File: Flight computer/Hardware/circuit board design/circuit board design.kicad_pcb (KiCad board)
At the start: 4 copper layers, 30.5 x 82.6 mm, 91 parts, among them J1 Conn_01x05, J2 USB_B_Micro, J3 Screw_Terminal_01x04, J4 Conn_01x02, J5 Screw_Terminal_01x04, J6 Conn_Coaxial, J7 Conn_Coaxial, SW1 SW_DPST, U1 IIS2MDC, U10 BMI088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

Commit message: Done extensive routing of the board.
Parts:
- removed SW1: SW_DPST, flight-computer:TerminalBlock_TE_282834-4_1x04_P2.54mm_Horizontal
- J3, J5: value Screw_Terminal_01x04 -> Screw_Terminal_01x06; footprint flight-computer:TerminalBlock_TE_282834-4_1x04_P2.54mm_Horizontal -> flight-computer:TerminalBlock_TE_282834-6_1x06_P2.54mm_Horizontal
- J4: moved to B.Cu
- moved R12 105.5 mm to (276.3, 306.1)
- moved R4 101.0 mm to (261.1, 292.1), turned to 180 degrees
- moved C86 98.8 mm to (266.1, 282.9), turned to 270 degrees
- moved C88 97.9 mm to (263.3, 285.5), turned to 270 degrees
- moved C89 97.9 mm to (276.3, 307.8), turned to 180 degrees
- moved R1 95.8 mm to (276.5, 297.1)
- moved C35 93.7 mm to (261.1, 290.4), turned to 180 degrees
- moved C7 91.1 mm to (276.4, 302.0), turned to 180 degrees
- moved Y3 90.8 mm to (263.8, 282.8), turned to 180 degrees
- moved C36 90.1 mm to (260.0, 283.6), turned to 90 degrees
- moved J1 87.7 mm to (279.8, 296.9)
- moved U15 87.7 mm to (260.9, 287.3), turned to 90 degrees
- moved R28 87.1 mm to (256.1, 277.6)
- moved R29 85.1 mm to (259.2, 277.6)
- moved J4 84.6 mm to (256.5, 287.3), turned to 90 degrees
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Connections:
- ANT1 pad 2: Net-(ANT1-Pad2) -> (no net)
- J2 pad 4: Net-(J2-Pad4) -> (no net)
- J3 pad 2: /pyro_driver/FET_B -> Vdrive
- J3 pad 4: /pyro_driver/FET_A -> /pyro_driver/FET_B
- U1 pad 11: Net-(U1-Pad11) -> (no net)
- U1 pad 12: Net-(U1-Pad12) -> (no net)
- U1 pad 2: Net-(U1-Pad2) -> (no net)
- U10 pad 1: Net-(U10-Pad1) -> (no net)
- U10 pad 13: Net-(U10-Pad13) -> (no net)
- U10 pad 5: Net-(U10-Pad5) -> (no net)
- U11 pad 10: Net-(U11-Pad10) -> (no net)
- U11 pad 12: Net-(U11-Pad12) -> (no net)
- U11 pad 17: /pyro_driver/FIRE_A -> /pyro_driver/FIRE_C
- U11 pad 18: /pyro_driver/FIRE_B -> /pyro_driver/FIRE_D
- U11 pad 19: /pyro_driver/FIRE_C -> /pyro_driver/FIRE_A
- U11 pad 20: /pyro_driver/FIRE_D -> /pyro_driver/FIRE_B
- U11 pad 38: Net-(U11-Pad38) -> (no net)
- U11 pad 39: Net-(U11-Pad39) -> (no net)
- U11 pad 5: Net-(U11-Pad5) -> (no net)
- U11 pad 51: Net-(U11-Pad51) -> (no net)
- U11 pad 55: Net-(U11-Pad55) -> (no net)
- U11 pad 59: Net-(U11-Pad59) -> (no net)
- U11 pad 6: Net-(U11-Pad6) -> (no net)
- U11 pad 60: Net-(U11-Pad60) -> (no net)
- U11 pad 9: Net-(U11-Pad9) -> (no net)
- U14 pad 4: Net-(U14-Pad4) -> (no net)
- U3 pad 10: /MCU/MCU_PA13 -> /MCU/MCU_PA12
- U3 pad 16: Net-(U3-Pad16) -> (no net)
- U3 pad 19: Net-(U3-Pad19) -> (no net)
- U3 pad 20: Net-(U3-Pad20) -> (no net)
- U3 pad 5: Net-(U3-Pad5) -> (no net)
- U3 pad 7: Net-(U3-Pad7) -> (no net)
- U3 pad 9: /MCU/MCU_PA12 -> /MCU/MCU_PA13
- U4 pad 13: Net-(U4-Pad13) -> (no net)
- U4 pad 15: Net-(U4-Pad15) -> (no net)
- U4 pad 5: Net-(U4-Pad5) -> (no net)
- U4 pad 6: Net-(U4-Pad6) -> (no net)
- U8 pad 6: Net-(U8-Pad6) -> (no net)
- X1 pad 1: Net-(X1-Pad1) -> (no net)
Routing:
- net Net-(J3-Pad1): track 0.00 -> 162.0 mm
- net /gps/GPS_SCL: track 0.20 -> 59.6 mm, vias 0 -> 2
- net /gps/GPS_NSAFEBOOT: track 0.00 -> 46.9 mm
- net /sensors/ACCL_RDY: track 0.00 -> 44.5 mm, vias 0 -> 2
- net GND: track 106.6 -> 150.8 mm, vias 35 -> 58
- net /gps/GPS_NRES: track 0.00 -> 39.6 mm, vias 0 -> 2
- net /sensors/GYRO_RDY: track 0.00 -> 38.6 mm, vias 0 -> 2
- net /pyro_driver/FIRE_A: track 0.00 -> 38.2 mm, vias 0 -> 2
- net /MCU/MCU_SCLK4: track 0.00 -> 37.1 mm, vias 0 -> 2
- net /MCU/MCU_PA04: track 0.00 -> 34.3 mm, vias 0 -> 2
- net /MCU/MCU_PB11: track 0.00 -> 33.1 mm, vias 0 -> 2
- net /pyro_driver/FIRE_B: track 0.00 -> 32.9 mm, vias 0 -> 2
- net /MCU/GPS_RXD0: track 0.00 -> 29.4 mm
- net /MCU/ARMED: track 0.00 -> 28.8 mm, vias 0 -> 1
- net Net-(C89-Pad1): track 0.00 -> 27.6 mm, vias 0 -> 2
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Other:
- outline, holes or cut-outs redrawn

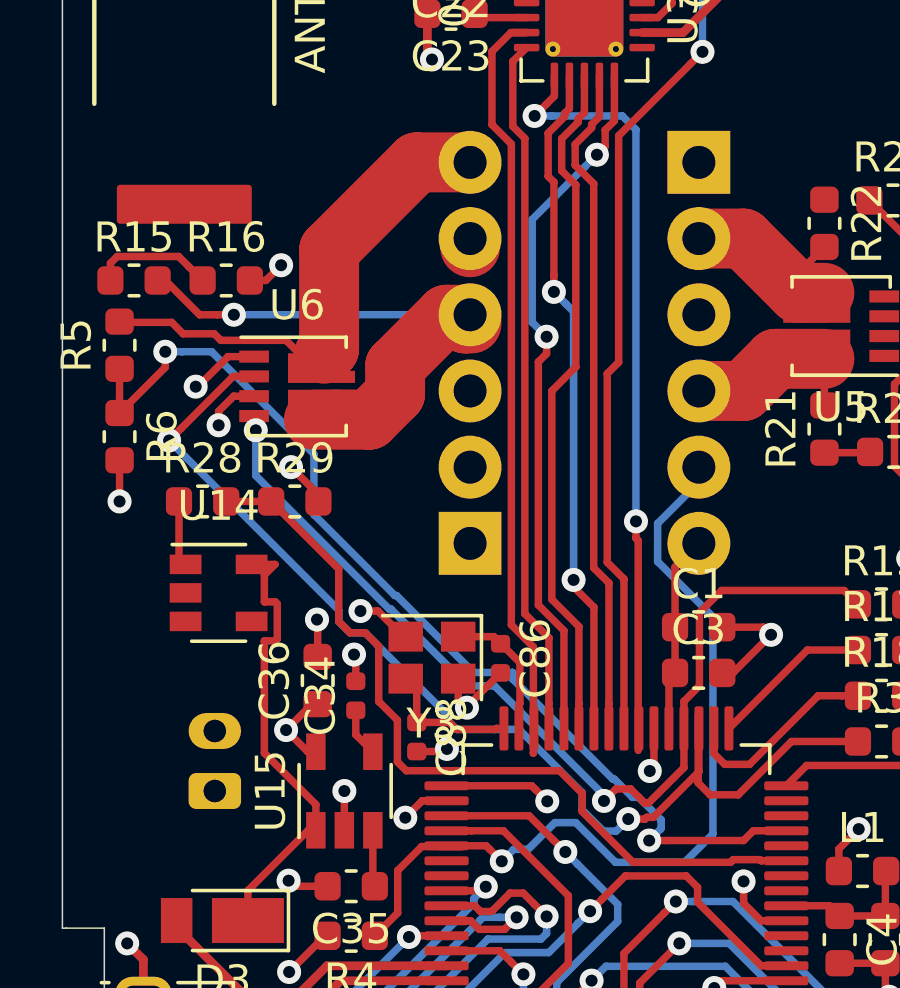
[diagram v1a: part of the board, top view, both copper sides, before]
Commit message: Set up for arming switch
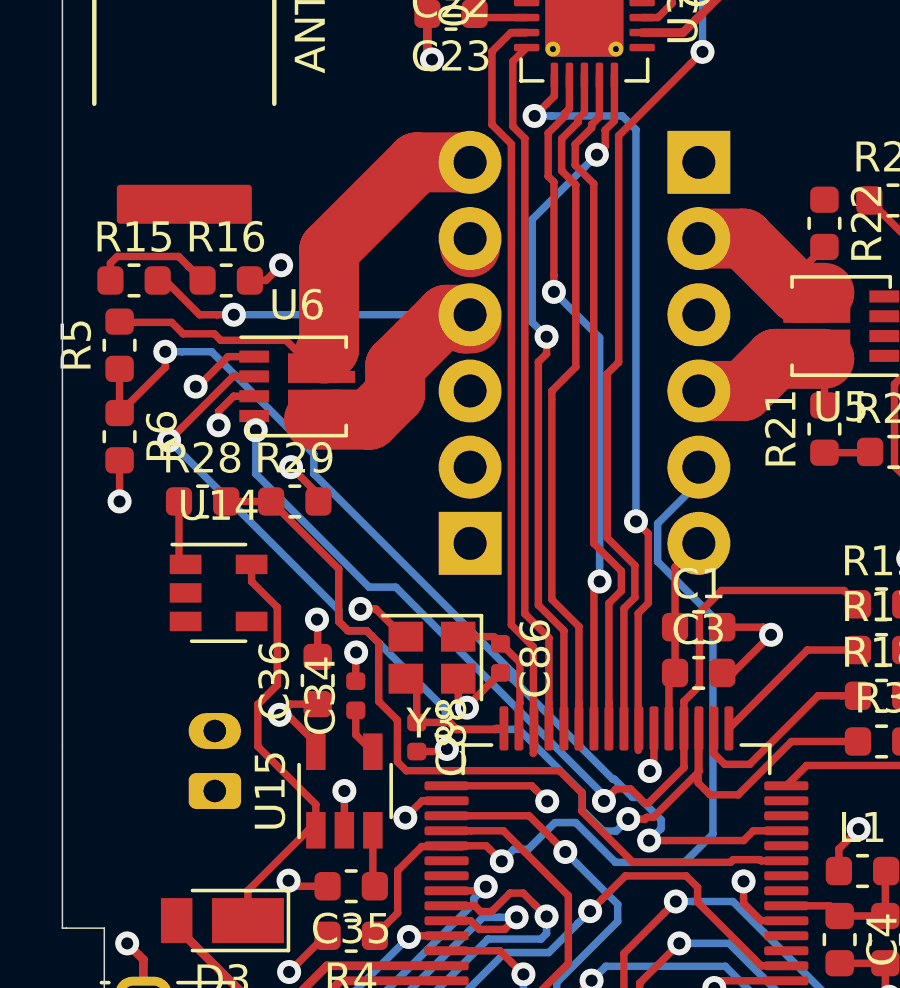
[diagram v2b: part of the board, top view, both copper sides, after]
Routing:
- net Net-(J3-Pad1): track 162.0 -> 0.29 mm
- net Vdrive: track 2.19 -> 24.7 mm
- net Net-(C35-Pad1): track 17.3 -> 16.3 mm
- net /MCU/MCU_PA04: track 34.3 -> 33.5 mm
- net +3V3: track 81.9 -> 82.5 mm

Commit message: only 2 or 3 connections left to route
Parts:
- removed R4: 1K, Resistor_SMD:R_0603_1608Metric
- J3, J5: value Screw_Terminal_01x06 -> Screw_Terminal_01x04; footprint flight-computer:TerminalBlock_TE_282834-6_1x06_P2.54mm_Horizontal -> flight-computer:TerminalBlock_TE_282834-4_1x04_P2.54mm_Horizontal
- moved R2 4.10 mm to (265.8, 322.7), turned to 90 degrees
- moved J5 2.79 mm to (272.7, 269.1)
- moved R21 2.47 mm to (276.4, 277.6), turned to 270 degrees
- moved J3 2.29 mm to (264.9, 276.7)
- moved R23 2.10 mm to (277.9, 277.6), turned to 270 degrees
- moved C8 1.53 mm to (264.8, 322.7)
- moved L8 1.42 mm to (264.3, 257.6)
- moved C22 1.42 mm to (263.0, 259.3)
- moved C9 1.42 mm to (268.6, 252.3)
- moved U3 1.42 mm to (267.5, 261.2)
- moved X1 1.42 mm to (273.9, 256.7)
- moved C19 1.42 mm to (263.4, 255.8)
- moved U2 1.42 mm to (267.6, 255.9)
- moved C20 1.42 mm to (272.4, 259.6)
- moved C21 1.42 mm to (276.2, 256.9)
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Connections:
- J3 pad 1: Net-(J3-Pad1) -> Vdrive
- J3 pad 2: Vdrive -> /pyro_driver/FET_B
- J3 pad 3: Net-(J3-Pad1) -> Vdrive
- J3 pad 4: /pyro_driver/FET_B -> /pyro_driver/FET_A
- J5 pad 1: Net-(J3-Pad1) -> Vdrive
- J5 pad 3: Net-(J3-Pad1) -> Vdrive
- U11 pad 37: /MCU/ARMED -> (no net)
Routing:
- net +3V3: track 82.5 -> 257.7 mm, vias 21 -> 25
- net /MCU/MCU_PA05: track 4.07 -> 33.9 mm, vias 0 -> 2
- net /MCU/ARMED: track 28.8 -> 0.00 mm, vias 1 -> 0
- net Vdrive: track 24.7 -> 5.46 mm, vias 0 -> 2
- net /pyro_driver/FIRE_D: track 6.73 -> 24.2 mm, vias 0 -> 2
- net /MCU/MCU_PA06: track 1.53 -> 18.5 mm, vias 0 -> 2
- net /pyro_driver/FIRE_C: track 5.38 -> 19.7 mm, vias 0 -> 2
- net /pyro_driver/FET_B: track 18.7 -> 4.94 mm, vias 1 -> 0
- net GND: track 150.9 -> 163.8 mm, vias 58 -> 66
- net Net-(C9-Pad1): track 0.00 -> 7.17 mm
- net /MCU/MCU_SCLK4: track 37.1 -> 30.9 mm
- net Net-(C8-Pad1): track 6.56 -> 2.10 mm
- net /pyro_driver/FET_C: track 6.66 -> 10.4 mm
- net Net-(R2-Pad2): track 6.93 -> 3.25 mm
- net /pyro_driver/FET_A: track 16.6 -> 13.7 mm
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- added copper zone on VCC.Cu, net Vdrive
- removed copper zone on VCC.Cu, net +3V3

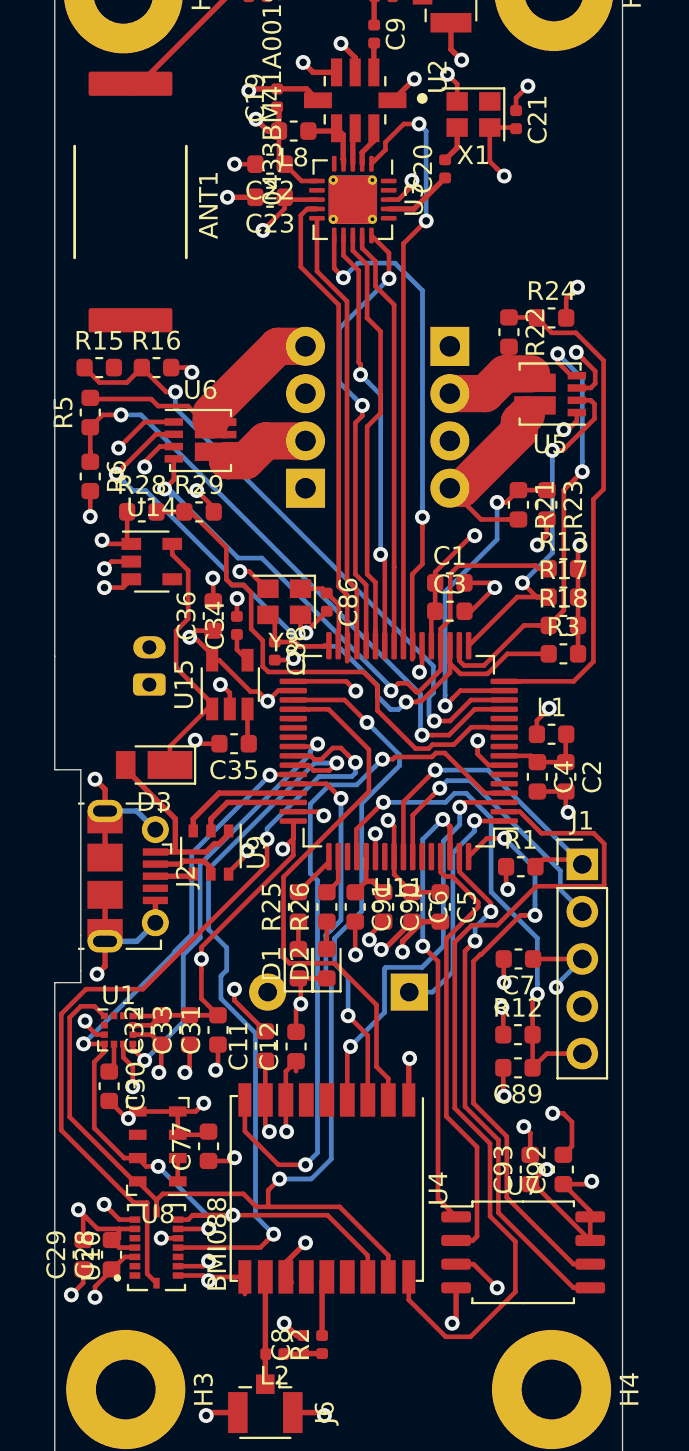
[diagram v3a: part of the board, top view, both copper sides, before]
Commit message: All connections routed!!
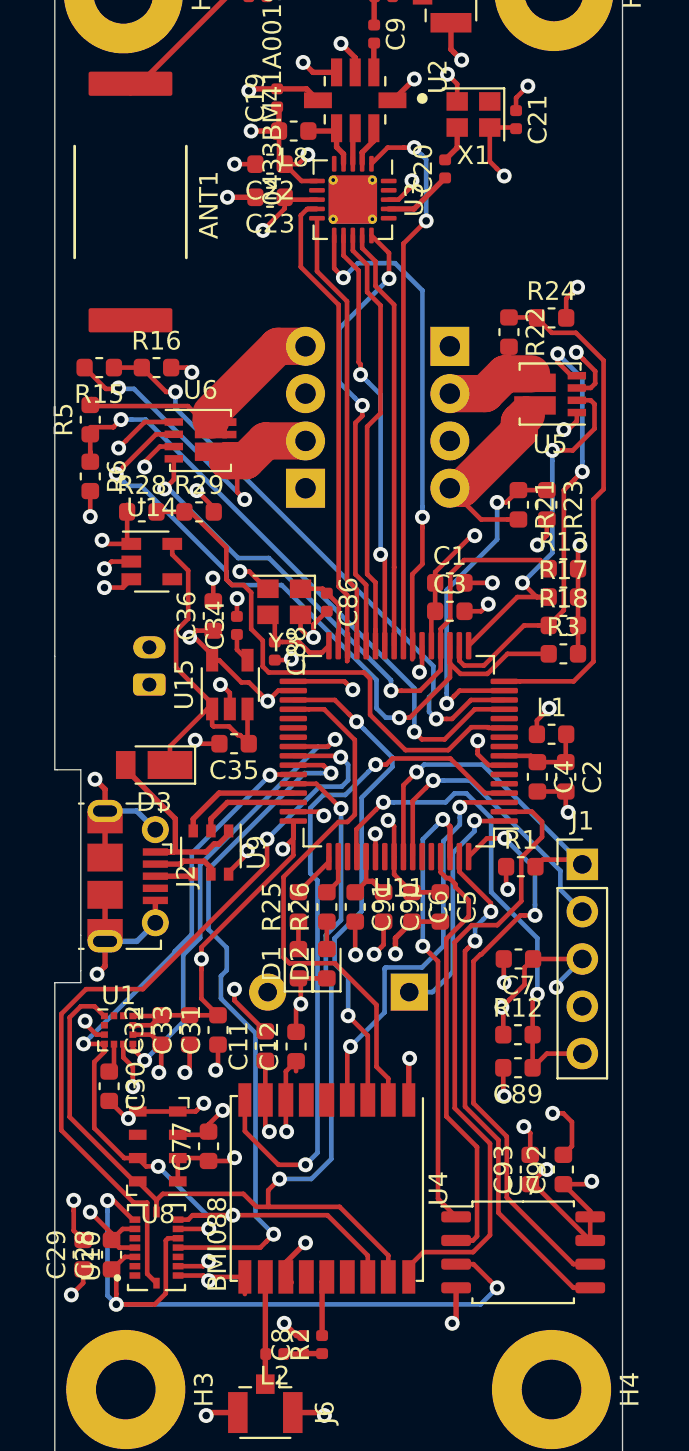
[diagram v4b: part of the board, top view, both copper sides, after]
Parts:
- moved R5 0.38 mm to (253.4, 273.1)
- turned R15 to 180 degrees
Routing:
- net +3V3: track 257.7 -> 302.9 mm
- net /pyro_driver/FET_B: track 4.94 -> 18.7 mm, vias 0 -> 2
- net /gps/GPS_NSAFEBOOT: track 46.5 -> 33.6 mm
- net Net-(C35-Pad1): track 16.3 -> 19.5 mm
- net /MCU/MCU_PA05: track 33.9 -> 31.7 mm
- net /MCU/MCU_PB11: track 32.4 -> 30.2 mm
- net /sensors/MAG_RDY: track 23.4 -> 25.3 mm
- net GND: track 163.8 -> 162.2 mm, vias 66 -> 68
- net /sensors/ACCL_RDY: track 43.8 -> 42.4 mm
- net /sensors/GYRO_RDY: track 38.6 -> 37.6 mm
- net /pyro_driver/FIRE_A: track 37.6 -> 38.4 mm
- net /MCU/SWCLK: track 18.4 -> 19.1 mm
- net (no net): track 0.76 -> 0.00 mm
- net /gps/GPS_RXD: track 27.6 -> 27.0 mm
- net /MCU/MCU_MISO4: track 24.1 -> 23.5 mm

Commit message: cleaned up redundent overlapping tracks
also added a 4 header pins for unused mcu pins to the circuit. Not added to board layout yet.
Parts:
- moved C20 246.8 mm to (113.3, 71.0)
- moved C21 246.8 mm to (117.1, 68.3)
- moved C88 246.8 mm to (104.1, 96.9)
- moved C89 246.8 mm to (117.2, 119.3)
- moved C93 246.8 mm to (117.9, 124.7)
- moved R5 246.8 mm to (94.2, 84.5)
- moved R6 246.8 mm to (94.2, 87.5)
- moved U11 246.8 mm to (110.8, 102.3)
- moved BZ1 246.8 mm to (111.4, 115.2)
- moved C10 246.8 mm to (102.7, 60.1)
- moved C8 246.8 mm to (105.7, 134.1)
- moved C9 246.8 mm to (109.5, 63.8)
- moved H3 246.8 mm to (96.1, 136.5)
- moved J3 246.8 mm to (105.8, 88.1)
- moved J4 246.8 mm to (97.4, 98.7)
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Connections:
- U11 pad 10: (no net) -> Net-(J8-Pad4)
- U11 pad 5: (no net) -> Net-(J8-Pad1)
- U11 pad 6: (no net) -> Net-(J8-Pad2)
- U11 pad 9: (no net) -> Net-(J8-Pad3)
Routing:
- net GND: track 162.2 -> 159.4 mm, vias 68 -> 67
- net +3V3: track 302.9 -> 300.9 mm, vias 25 -> 24
- net Net-(C9-Pad1): track 7.17 -> 8.33 mm

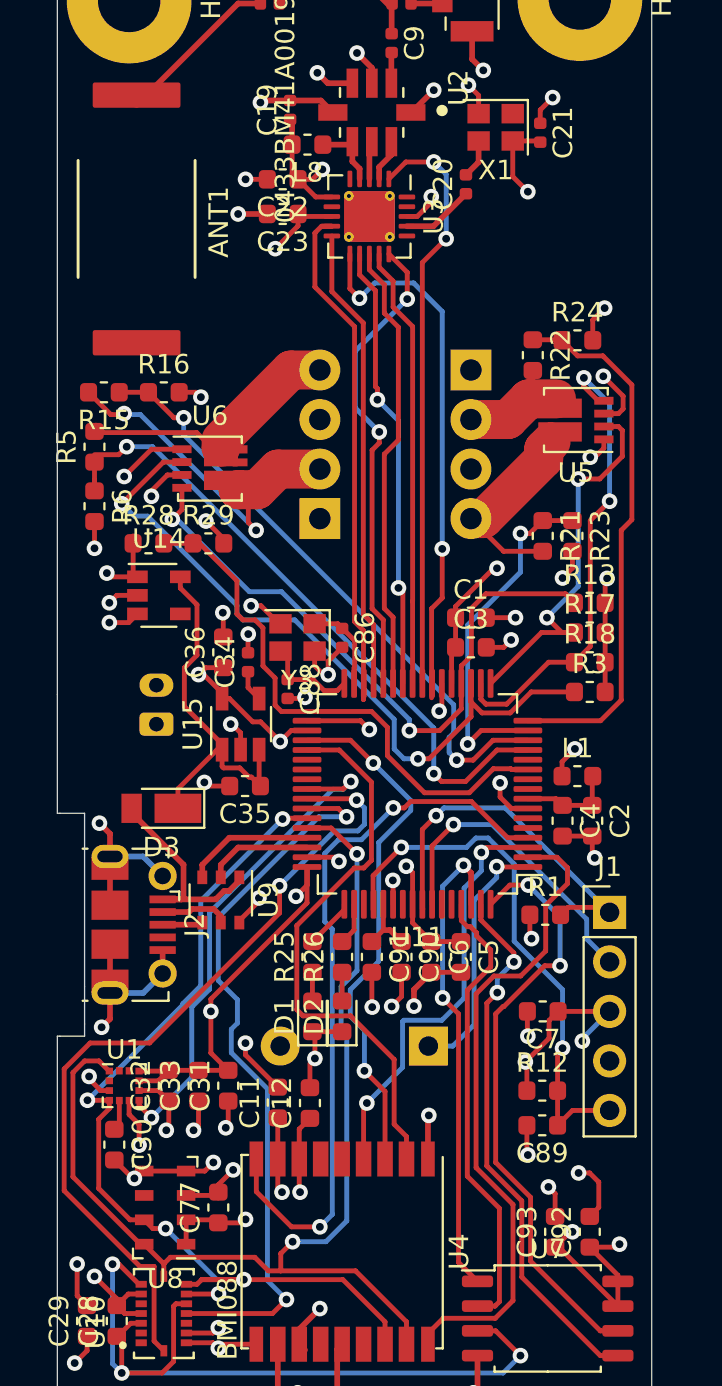
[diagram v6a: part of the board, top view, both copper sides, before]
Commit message: added in molex usb 3D cad and silk screen ICSS logo
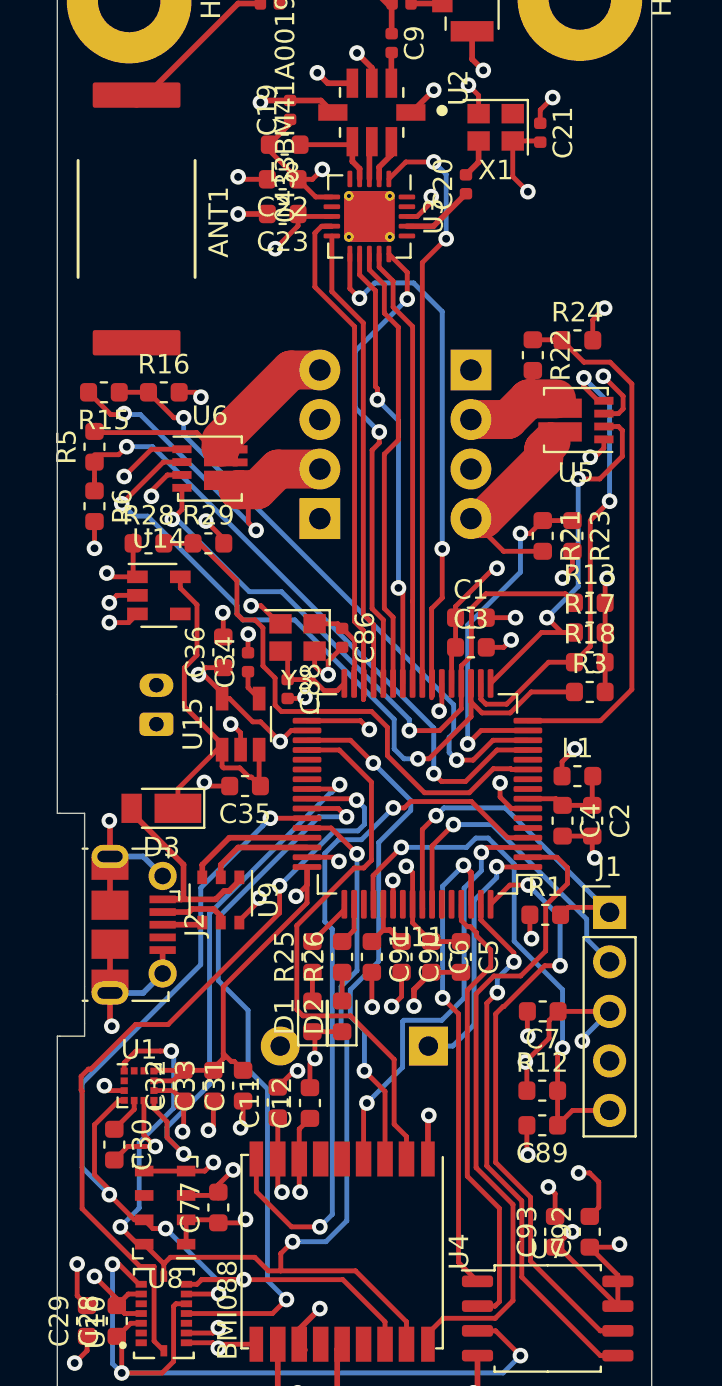
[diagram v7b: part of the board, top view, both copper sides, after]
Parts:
- ANT1: value ICSSPicoTracker_Yageo434 -> Yageo434; footprint pico_tracker:Yageo434 -> flight-computer:Yageo434
- J2: footprint Connector_USB:USB_Micro-B_Molex-105017-0001 -> flight-computer:USB_Micro-B_Molex-105017-0001
- moved L8 1.17 mm to (104.0, 69.0)
- moved C31 0.76 mm to (101.9, 117.2)
- moved C32 0.76 mm to (98.8, 117.2)
- moved C33 0.76 mm to (100.3, 117.2)
- moved U1 0.76 mm to (96.5, 117.2)
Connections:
- U11 pad 5: Net-(J8-Pad1) (its old number) -> (no net)
- U11 pad 6: Net-(J8-Pad2) (its old number) -> (no net)
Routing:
- net +3V3: track 300.9 -> 306.9 mm, vias 24 -> 23
- net /gps/GPS_SDA: track 49.6 -> 55.0 mm
- net /sensors/MAG_RDY: track 25.3 -> 28.1 mm
- net /gps/GPS_SCL: track 57.5 -> 59.8 mm, vias 2 -> 4
- net /sensors/ACCL_RDY: track 42.4 -> 40.9 mm
- net Net-(L8-Pad1): track 3.65 -> 4.82 mm
- net GND: track 159.4 -> 159.1 mm, vias 67 -> 66
